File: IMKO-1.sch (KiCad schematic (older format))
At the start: 6 parts, among them U1 8080, U2 8228, U3 8224, U40 74LS244, U41 74LS245

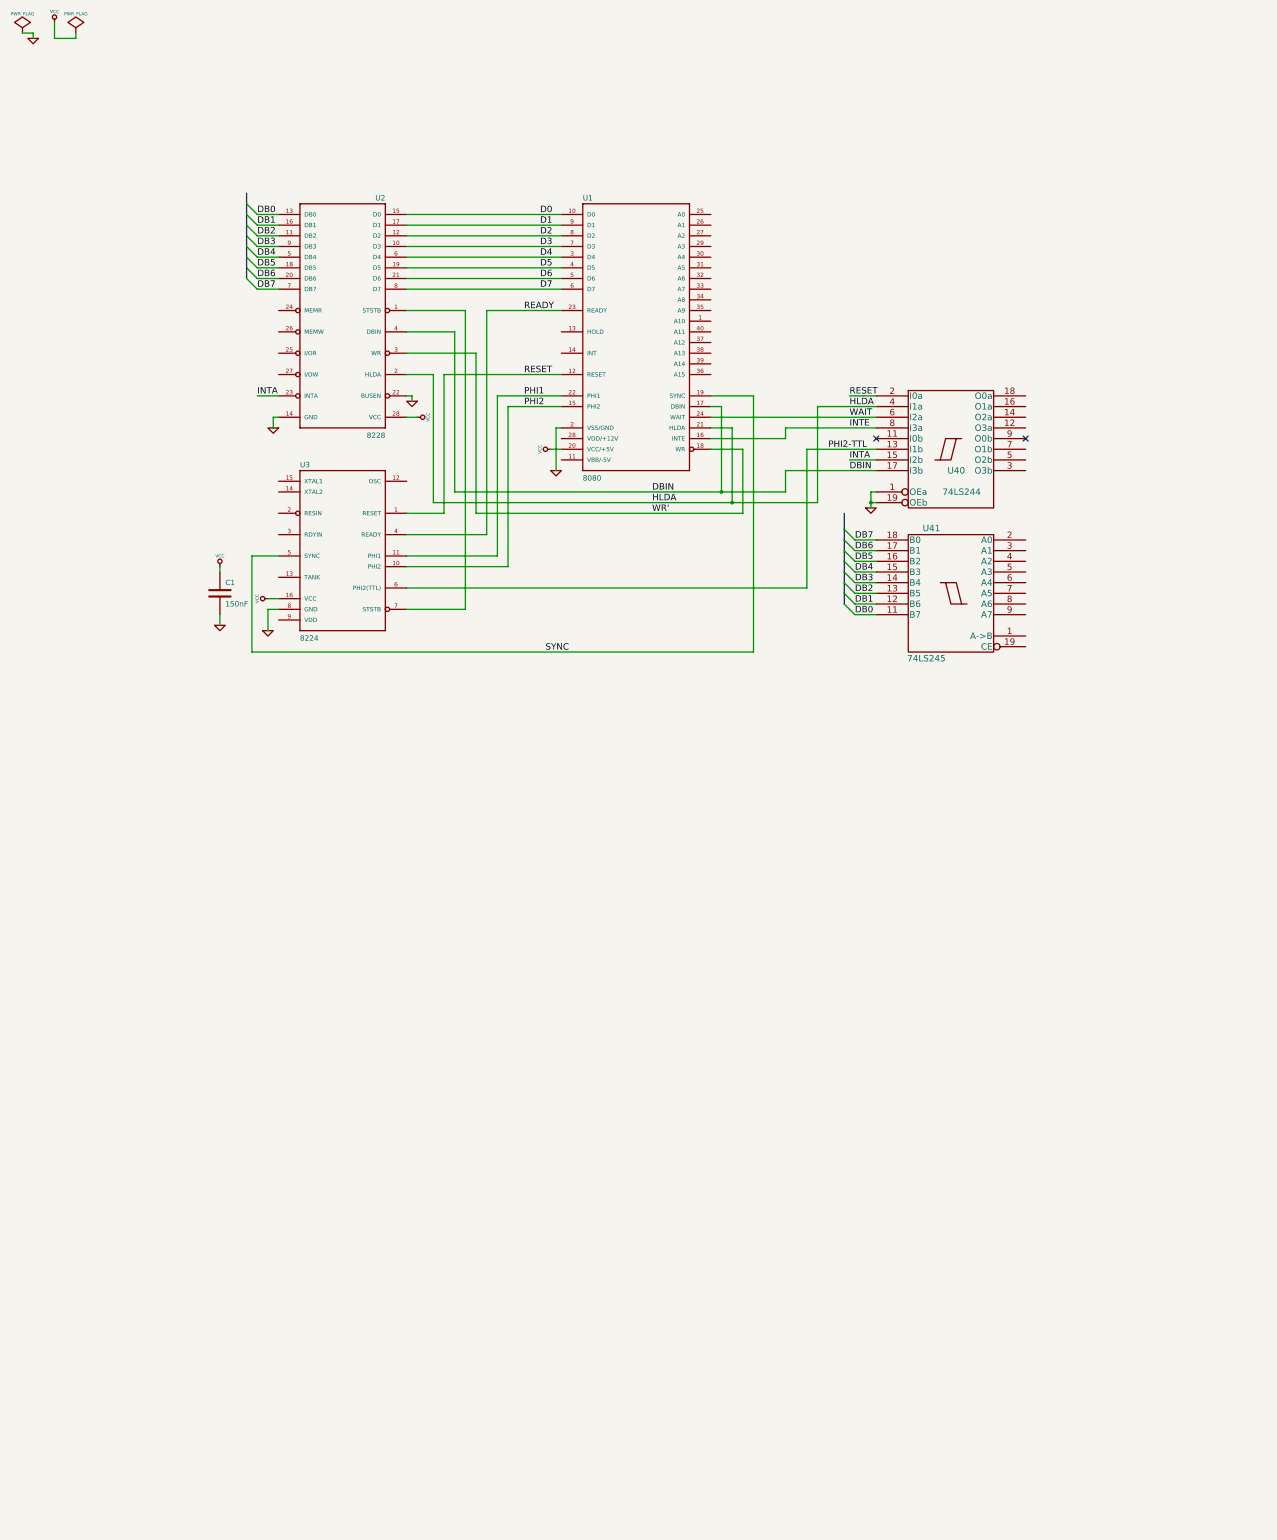
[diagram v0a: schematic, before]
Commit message: Added EPROMs
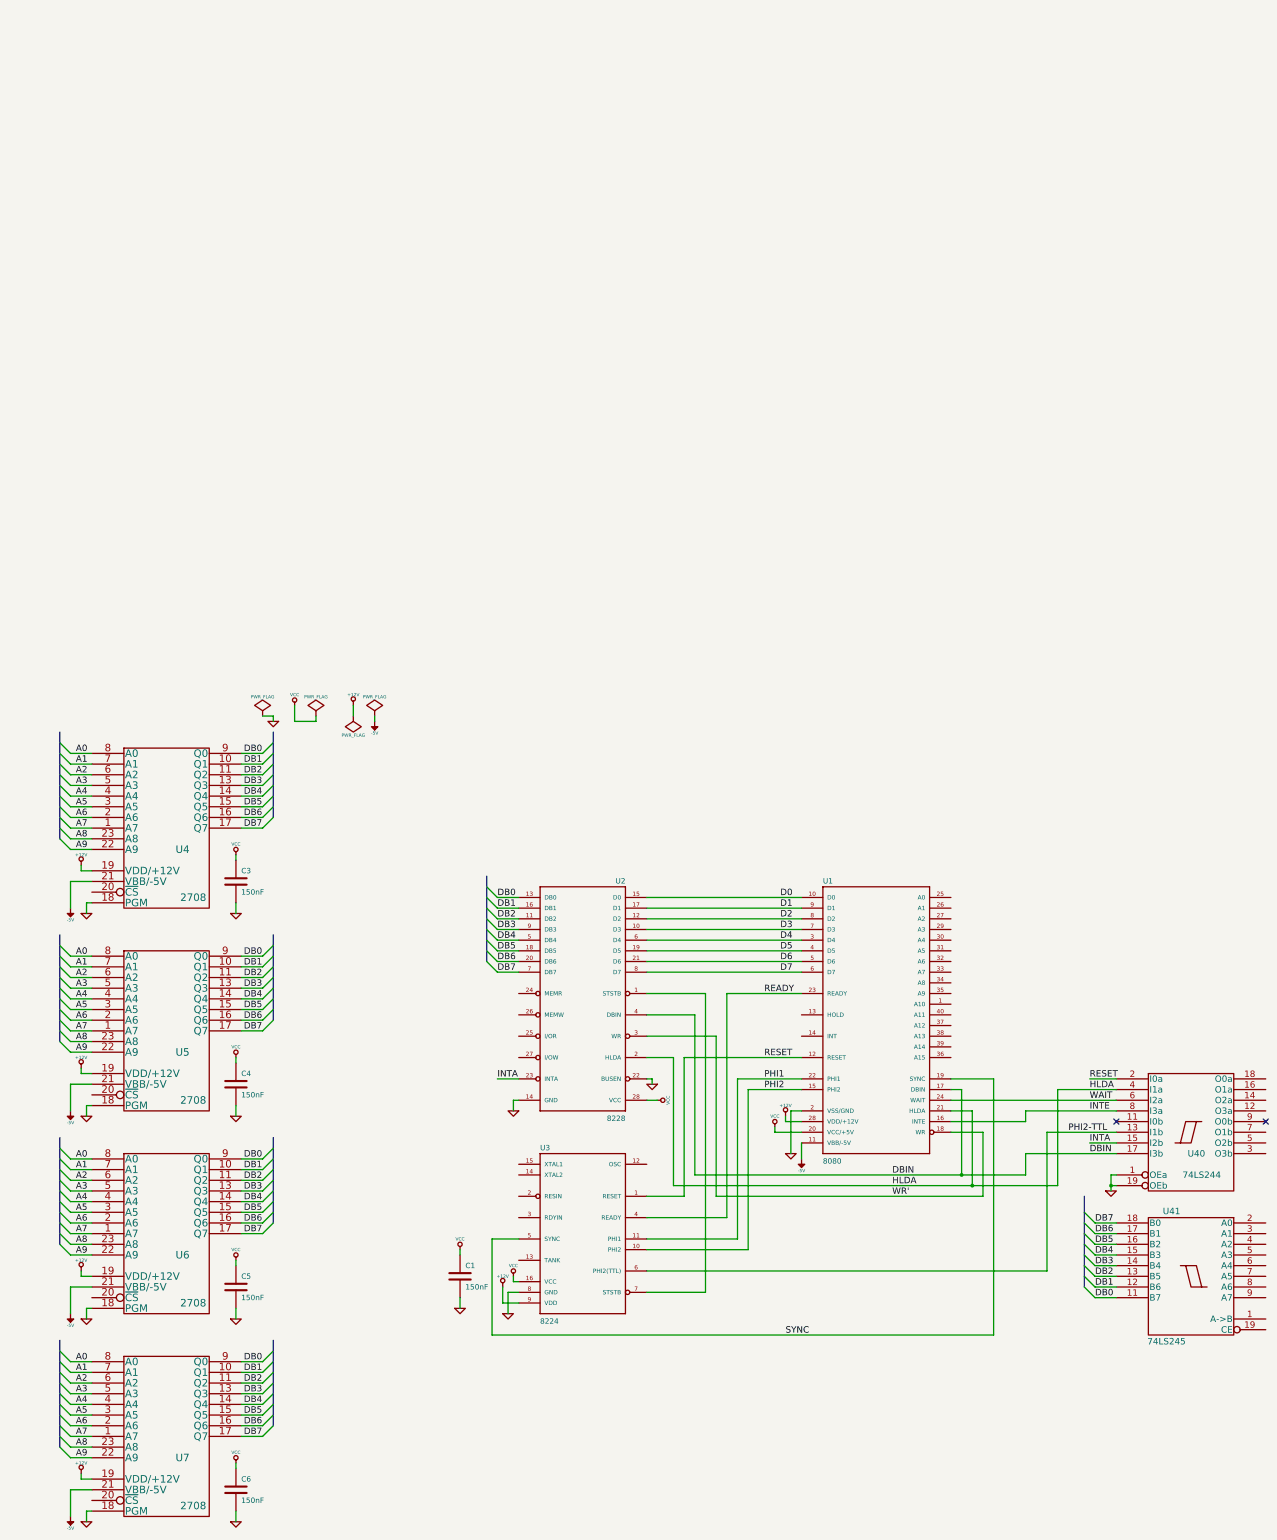
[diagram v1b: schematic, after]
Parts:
- added C3, C4, C5, C6: 150nF, symbol C
- added U4, U5, U6, U7: 2708, symbol 2708
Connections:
- net DB0: now also U4.9 (Q0), U5.9 (Q0), U6.9 (Q0), U7.9 (Q0)
- net DB1: now also U4.10 (Q1), U5.10 (Q1), U6.10 (Q1), U7.10 (Q1)
- net DB2: now also U4.11 (Q2), U5.11 (Q2), U6.11 (Q2), U7.11 (Q2)
- net DB3: now also U4.13 (Q3), U5.13 (Q3), U6.13 (Q3), U7.13 (Q3)
- net DB4: now also U4.14 (Q4), U5.14 (Q4), U6.14 (Q4), U7.14 (Q4)
- net DB5: now also U4.15 (Q5), U5.15 (Q5), U6.15 (Q5), U7.15 (Q5)
- net DB6: now also U4.16 (Q6), U5.16 (Q6), U6.16 (Q6), U7.16 (Q6)
- net DB7: now also U4.17 (Q7), U5.17 (Q7), U6.17 (Q7), U7.17 (Q7)
- net GND: now also C3.2, C4.2, C5.2, C6.2, U4.12 (GND), U4.18 (PGM), U5.12 (GND), U5.18 (PGM), U6.12 (GND), U6.18 (PGM), U7.12 (GND), U7.18 (PGM)
- net VCC: now also C3.1, C4.1, C5.1, C6.1
- net -5V: now reaches U1.11 (VBB/-5V)
- net -5V: now also U4.21 (VBB/-5V), U5.21 (VBB/-5V), U6.21 (VBB/-5V), U7.21 (VBB/-5V)
- net +12V: now reaches U1.28 (VDD/+12V)
- net +12V: now also U3.9 (VDD), U4.19 (VDD/+12V), U5.19 (VDD/+12V), U6.19 (VDD/+12V), U7.19 (VDD/+12V)
- new net A0: U4.8 (A0), U5.8 (A0), U6.8 (A0), U7.8 (A0)
- new net A1: U4.7 (A1), U5.7 (A1), U6.7 (A1), U7.7 (A1)
- new net A2: U4.6 (A2), U5.6 (A2), U6.6 (A2), U7.6 (A2)
- new net A3: U4.5 (A3), U5.5 (A3), U6.5 (A3), U7.5 (A3)
- new net A4: U4.4 (A4), U5.4 (A4), U6.4 (A4), U7.4 (A4)
- new net A5: U4.3 (A5), U5.3 (A5), U6.3 (A5), U7.3 (A5)
- new net A6: U4.2 (A6), U5.2 (A6), U6.2 (A6), U7.2 (A6)
- new net A7: U4.1 (A7), U5.1 (A7), U6.1 (A7), U7.1 (A7)
- new net A8: U4.23 (A8), U5.23 (A8), U6.23 (A8), U7.23 (A8)
- new net A9: U4.22 (A9), U5.22 (A9), U6.22 (A9), U7.22 (A9)
- new net Vcc: U4.24 (Vcc), U5.24 (Vcc), U6.24 (Vcc), U7.24 (Vcc)
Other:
- moved on the sheet: C1, U1, U2, U3, U40, U41

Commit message: Added address buffers and EPROM chip-select
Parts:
- added C2: 10pF, symbol C
- added PLACEHOLDER1: CONN_10, symbol CONN_10
- added R1: 22k, symbol R
- added R2, R4: 1k, symbol R
- added R3: 10k, symbol R
- added U33: 74LS138, symbol 74LS138
- added U34: 74LS32, symbol 74LS32
- added U35: 74LS00, symbol 74LS00
- added U38, U39: 74LS244, symbol 74LS244
- added X1: 18MHz, symbol CRYSTAL
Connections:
- net labels added: A10, A11, A12, A13, A14, AA0, AA1, AA10, AA11, AA12, AA13, AA14, AA15, AA2, AA3, AA4, AA5, AA6, AA7, AA8, AA9, HOLD, INT, RDYIN, RESIN, STSTB, ~A15, ~AA15, ~CE_U41, ~CS_EPR0, ~CS_EPR1, ~CS_EPR2, ~CS_EPR3, ~MEMR
- wire segments 207 -> 346
- no-connect marks 2 -> 7
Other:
- moved on the sheet: U40, U41

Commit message: Added memory modules
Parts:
- added C10, C11, C12, C7, C8, C9: 150nF, symbol C
- added U27, U28, U29, U30, U31, U32: 2114, symbol 2114
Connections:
- net labels added: CS_RAM0, CS_RAM1, CS_RAM2, ~MEMW
- wire segments 346 -> 471
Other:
- moved on the sheet: U34A, U34B, U34C, U34D

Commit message: Added keyboard connector and ICs
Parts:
- added C33: ?, symbol CP1
- added P1: CONN_KBD, symbol CONN_8X2
- added R10, R11, R12, R13, R6, R7, R8, R9: 1k, symbol R
- added R5: 120, symbol R
- added U26: 74LS374, symbol 74LS374
- added U36: 74LS240, symbol 74LS240
- added U37: 74LS148, symbol 74LS148
- added U49: 74LS244, symbol 74LS244
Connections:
- net labels added: -12V, DBINX, KBD.D0, KBD.D1, KBD.D2, KBD.D3, KBD.D4, KBD.D5, KBD.D6, KBD.D7, KBD.RESIN
- wire segments 471 -> 571
- no-connect marks 7 -> 16
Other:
- note added: "TODO: Inputs?!"
- note added: "TODO: \nValue?!"
- moved on the sheet: R1, R2

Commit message: Added expansion slot
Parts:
- added J2: CONN_EXPANSION, 19inch-VG64, symbol VG64
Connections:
- net labels added: DBX0, DBX1, DBX2, DBX3, DBX4, DBX5, DBX6, DBX7, HLDAX, INTAX, INTEX, PHI2-TTLX, RESETX, TODO.U35.1, TODO.U37.1, TODO.U37.2, TODO.U37.3, TODO.U37.4, WAITX, ~IOR, ~IOW
- wire segments 571 -> 650
- no-connect marks 16 -> 25
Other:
- moved on the sheet: R3

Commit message: Cleanup, docs, canvas resize
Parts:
- removed PLACEHOLDER1: CONN_10, symbol CONN_10
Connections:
- net labels added: CS.RAM0, CS.RAM1, CS.RAM2, ~CE.U41, ~CS.EPROM0, ~CS.EPROM1, ~CS.EPROM2, ~CS.EPROM3
- net labels removed: CS_RAM0, CS_RAM1, CS_RAM2, ~CE_U41, ~CS_EPR0, ~CS_EPR1, ~CS_EPR2, ~CS_EPR3
- wire segments 650 -> 649
- no-connect marks 25 -> 16
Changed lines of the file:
@@
 encoding utf-8
 Sheet 1 1
-Title ""
-Date "23 sep 2012"
-Rev ""
-Comp ""
-Comment1 ""
+Title "IMKO-1 Personal Computer"
+Date "24 sep 2012"
+Rev "0.1"
+Comp "Released under the Creative Commons Attribution Share-Alike 3.0"
+Comment1 "Schematic and PCB capture by Dimitar Kovachev"
 Comment2 ""
 Comment3 ""
@@
 Text Label 8050 10700 0    60   ~ 0
 INT
-$Comp
-L CONN_10 PLACEHOLDER1
-U 1 1 505D8F7E
-P 14650 12250
-F 0 "PLACEHOLDER1" H 14600 11600 60  0000 C CNN
-F 1 "CONN_10" V 14700 12250 60  0000 C CNN
-	1    14650 12250
-	1    0    0    -1
-$EndComp
-Text Label 14100 12000 0    60   ~ 0
-INT
 Text Label 7000 13100 0    60   ~ 0
 STSTB
@@
 $EndComp
 Text Label 16700 10800 0    60   ~ 0
-~CS_EPR3
-Text Label 950  9350 0    60   ~ 0
-~CS_EPR3
+~CS.EPROM3
+Text Label 1350 9350 2    60   ~ 0
+~CS.EPROM3
 Text Label 16700 11300 0    60   ~ 0
-~CS_EPR2
-Text Label 950  11250 0    60   ~ 0
-~CS_EPR2
-Text Label 950  13150 0    60   ~ 0
-~CS_EPR1
+~CS.EPROM2
+Text Label 1350 11250 2    60   ~ 0
+~CS.EPROM2
+Text Label 1350 13150 2    60   ~ 0
+~CS.EPROM1
 Text Label 16700 10300 0    60   ~ 0
-~CS_EPR1
+~CS.EPROM1
 Text Label 16700 9800 0    60   ~ 0
-~CS_EPR0
-Text Label 950  15050 0    60   ~ 0
-~CS_EPR0
+~CS.EPROM0
+Text Label 1350 15050 2    60   ~ 0
+~CS.EPROM0
 Text Label 5350 10300 0    60   ~ 0
 ~MEMR
@@
 NoConn ~ 8300 7850
 Text Label 12650 14100 0    60   ~ 0
-~CE_U41
+~CE.U41
 Text Label 8350 8300 0    60   ~ 0
-~CE_U41
+~CE.U41
 $Comp
 L R R4
@@
 ~MEMW
 Text Label 14700 10300 0    60   ~ 0
-CS_RAM0
+CS.RAM0
 Text Label 14700 10400 0    60   ~ 0
-CS_RAM1
+CS.RAM1
 Text Label 14700 10500 0    60   ~ 0
-CS_RAM2
+CS.RAM2
 Text Label 5600 4400 0    60   ~ 0
-CS_RAM2
+CS.RAM2
 Text Label 3400 4400 0    60   ~ 0
-CS_RAM1
+CS.RAM1
 Text Label 1200 4400 0    60   ~ 0
-CS_RAM0
+CS.RAM0
 $Comp
 L 74LS240 U36
@@
 	21800 12650 21800 12550
 Wire Wire Line
-	14300 12000 14000 12000
-Wire Wire Line
 	8250 10700 7950 10700
 Wire Wire Line
@@
 Wire Wire Line
 	5800 8400 5450 8400
-NoConn ~ 14300 11900
-NoConn ~ 14300 12100
-NoConn ~ 14300 12200
-NoConn ~ 14300 12300
-NoConn ~ 14300 12400
-NoConn ~ 14300 12500
-NoConn ~ 14300 12600
-NoConn ~ 14300 12700
 Connection ~ 4450 12200
 $Comp
@@
 	21800 12000 21800 12050
 Connection ~ 21800 12000
-NoConn ~ 14300 11800
 Text Label 12650 11700 0    60   ~ 0
 HLDAX

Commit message: Added video sub-system. Power tracks fixes
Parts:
- added C13: 110pF, symbol C
- added C14: 68pF, symbol C
- added C15, C16, C17: 150nF, symbol C
- added C18: 68uF, symbol CP1
- added D1, D2: 1N4148, symbol DIODE
- added J9: CONN_VIDEO, symbol CONN_2
- added R14: 5k1, symbol R
- added R15: 3k3, symbol R
- added R16, R19, R23, R24, R25, R26, R27, R28, R29, R30, R31, R32, R33, R34: 1k, symbol R
- added R17: 120, symbol R
- added R18: 470, symbol R
- added R20: 240, symbol R
- added R22: 2M7, symbol R
- added T3: CONN_6, symbol CONN_6
- added T4: CONN_1, symbol CONN_1
- added U11, U12: 2114, symbol 2114
- added U13: 74LS374, symbol 74LS374
- added U14: 74LS165, symbol 74LS165
- added U15, U16, U19, U20: 74LS244, symbol 74LS244
- added U17: 74LS367, symbol 74LS367
- added U18: 82S129, symbol 82S129
- added U21: 74LS08, symbol 74LS08
- added U22: 74LS32, symbol 74LS32
- added U23: 74LS86, symbol 74LS86
- added U24: 74LS163, symbol 74LS163
- added U25: 74LS00, symbol 74LS00
- added U55: DIL20, symbol DIL20
- added U8: SFF96364, MODULE, symbol SFF96364
- added U9: RO-3-2513, MODULE, symbol RO-3-2513
- added VR1: POT, symbol POT
- added X2: 1MHz, symbol CRYSTAL
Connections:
- net labels added: CHR.A0, CHR.A1, CHR.A2, CHR.A3, CHR.A4, CHR.A5, CHR.D6, CHR.Q7, CHR0, CHR1, CHR2, CHR3, CHR4, CHR5, CHR6, CHR7, CS.CASS, NET1, OUT.INH, PROM.D4, SFF.A0, SFF.A1, SFF.A2, SFF.A3, SFF.A4, SFF.A5, SFF.A6, SFF.A7, SFF.A8, SFF.A9, SFF.CTRL0, SFF.CTRL1, SFF.CTRL2, SFF.PHI1, SFF.PT, SFF.RO0, SFF.RO1, SFF.RO2, SFF.SYNC, SFF.W, TMP.V1, TMP.V10, TMP.V2, TMP.V3, TMP.V4, TMP.V5, TMP.V6, TMP.V7, TMP.V8, TMP.V9, U19.EN, U20.EN, U23.8, U24.TC, U25.8, U42.NQ, U42.Q, U51.10, U55.11, U55.15, U55.6, U55.9, V.D0, V.D1, V.D2, V.D3, V.D4, V.D5, V.D6, V.D7, VID.A0, VID.A1, VID.A2, VID.A3, VID.A4, VID.A5, VID.A6, VID.A7, VID.A8, VID.A9, VID.D0, VID.D1, VID.D2, VID.D3, VID.D4, VID.D5, VID.D6, VID.LOAD, VID.SHIFT, VSYNC, ~SFF.INI, ~SFF.SYNC, ~VID.MEMW
- wire segments 649 -> 1046
- no-connect marks 16 -> 26
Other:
- note added: "Placeholder signals"
- note added: "TODO: Name"
- note added: "TODO: Name?"
- note added: "TODO: No D7?"
- note added: "TODO: Signal names"
- note added: "TODO: Value?"
- moved on the sheet: U34A, U34B, U34C, U34D

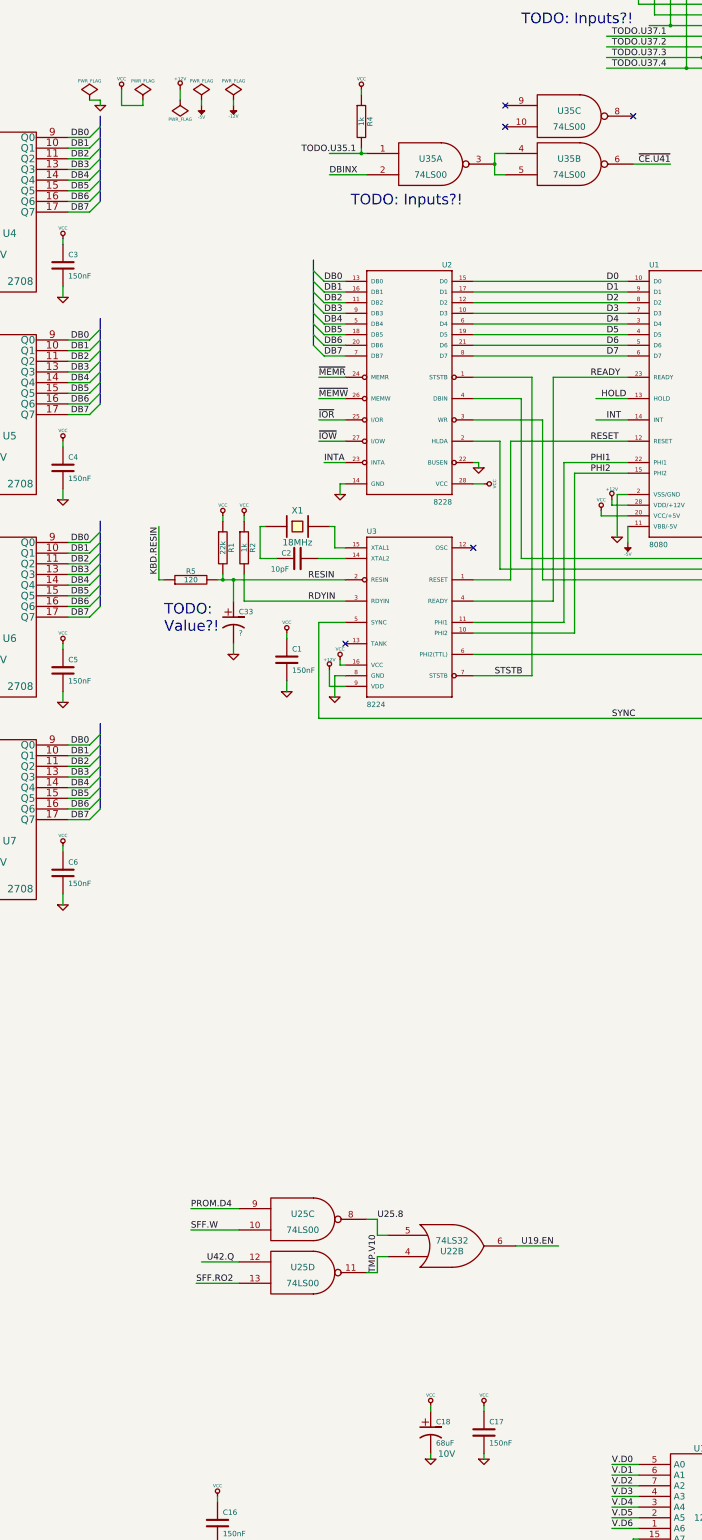
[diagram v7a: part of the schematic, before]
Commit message: Added power connector
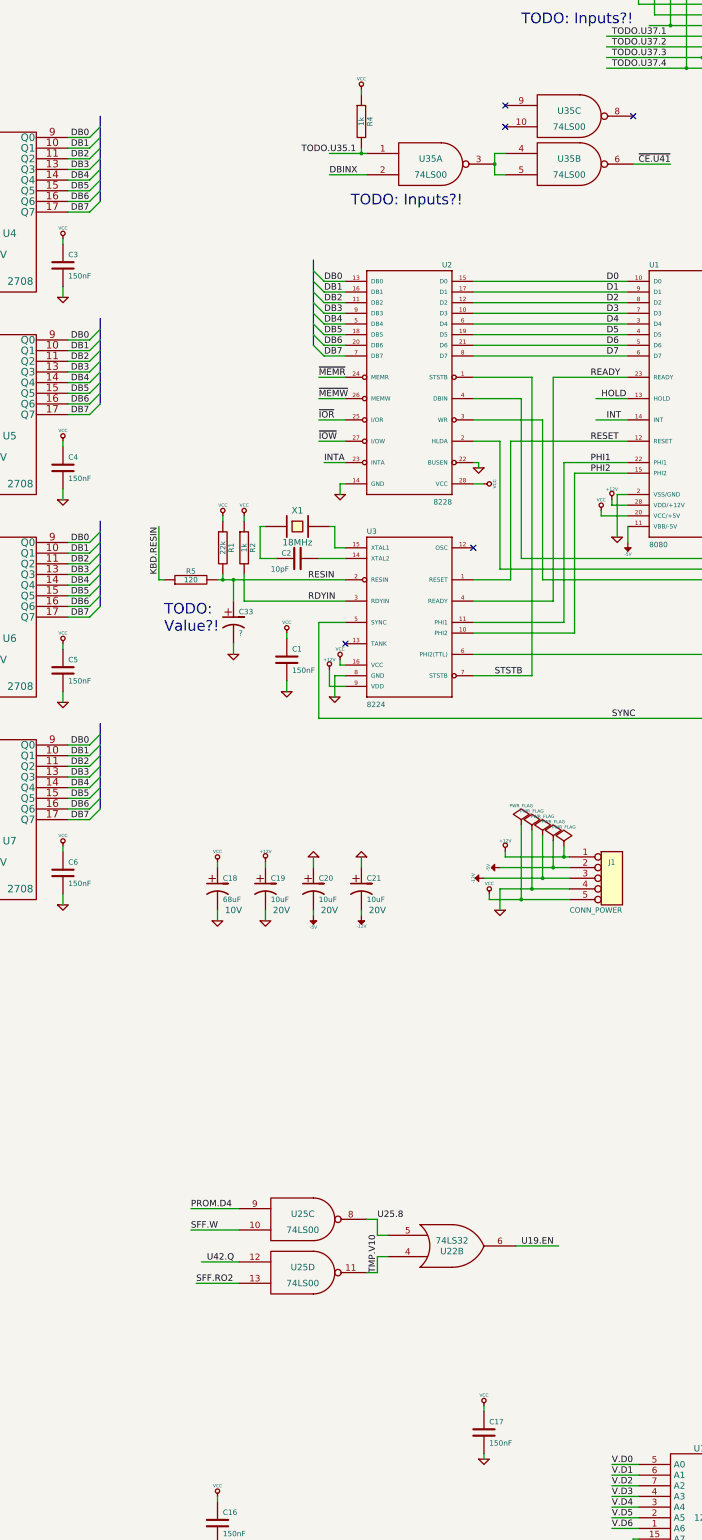
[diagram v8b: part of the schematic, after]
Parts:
- added C19, C20, C21: 10uF, symbol CP1
- added J1: CONN_POWER, symbol CONN_5
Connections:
- wire segments 1046 -> 1057
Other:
- moved on the sheet: C18
